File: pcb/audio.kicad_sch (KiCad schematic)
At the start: 30 parts, among them J4 AudioJack4, U4 ES7210, U5 ES8311, U6 IS31AP2005

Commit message: pcb: 473 cannot defeat me in any way that matters
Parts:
- J4: footprint Connector_Audio:Jack_3.5mm_PJ320D_Horizontal -> live-caption-badge:Jack_3.5mm_PJ320D_Horizontal
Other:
- title: (none) -> Live Caption Badge - Audio Subsystem
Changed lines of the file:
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@@
 	(generator_version "8.0")
 	(paper "A4")
+	(title_block
+		(title "Live Caption Badge - Audio Subsystem")
+		(date "2024-10-29")
+	)
 	(junction
 		(at 46.99 71.12)
@@
 			)
 		)
-		(property "Footprint" "Connector_Audio:Jack_3.5mm_PJ320D_Horizontal"
+		(property "Footprint" "live-caption-badge:Jack_3.5mm_PJ320D_Horizontal"
 			(at 158.75 129.54 0)
 			(effects

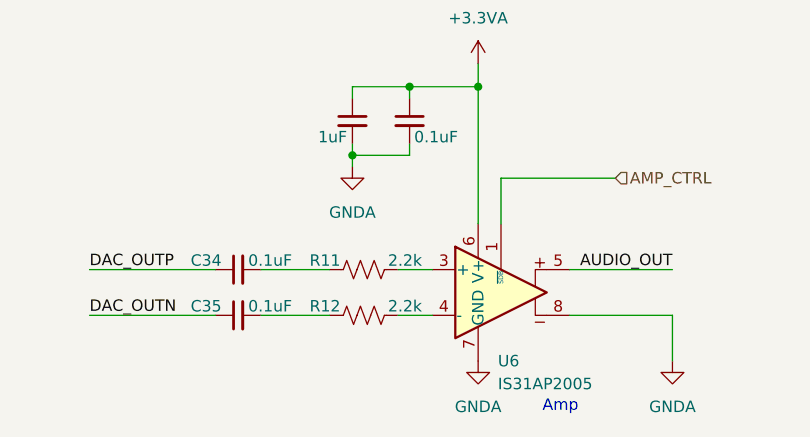
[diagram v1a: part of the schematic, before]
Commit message: pcb: Fix misc footprints, add silkprint
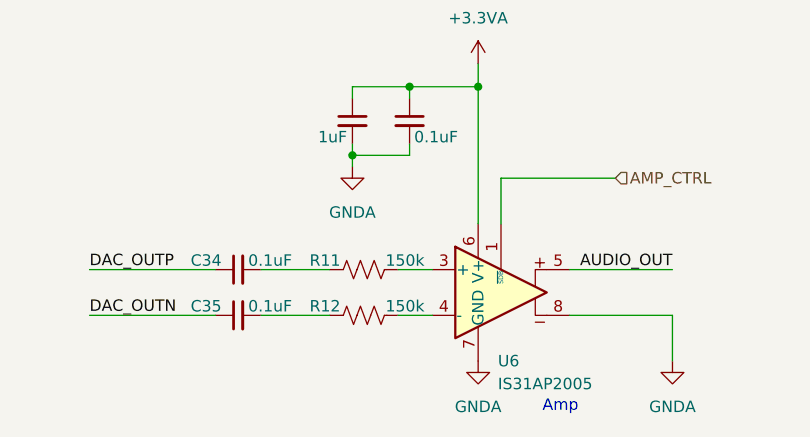
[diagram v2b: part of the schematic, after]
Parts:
- R11, R12: value 2.2k -> 150k
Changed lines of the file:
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@@
 			)
 		)
-		(property "Value" "2.2k"
+		(property "Value" "150k"
 			(at 78.232 141.224 90)
 			(effects
@@
 			)
 		)
-		(property "Value" "2.2k"
+		(property "Value" "150k"
 			(at 78.232 136.144 90)
 			(effects

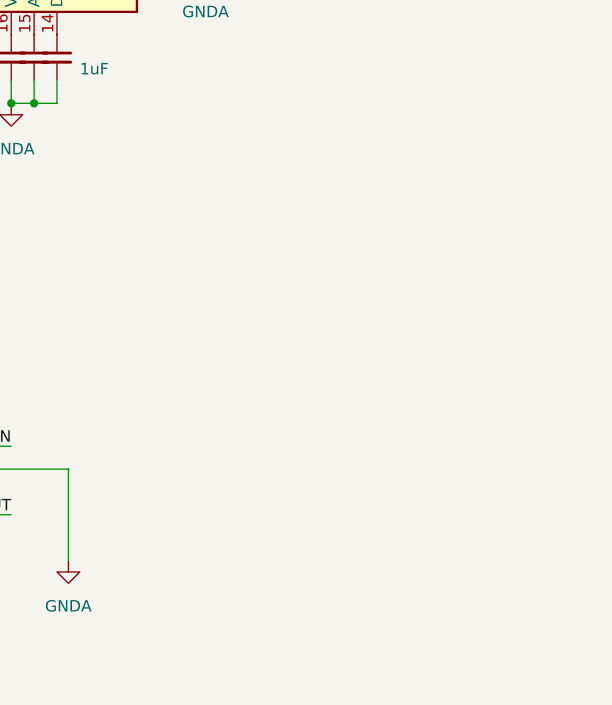
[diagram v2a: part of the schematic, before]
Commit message: pcb: Checkpoint before incorporating Mark and James' suggestions
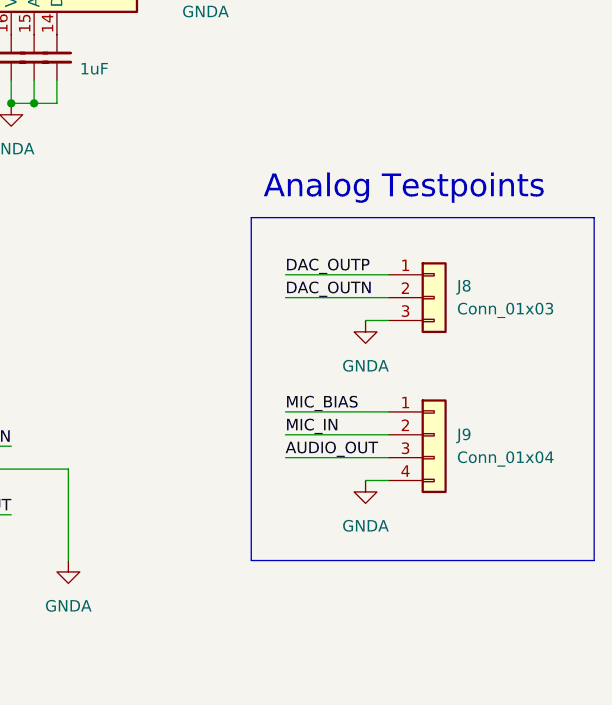
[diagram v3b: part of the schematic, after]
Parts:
- added J8: Conn_01x03, Connector_PinHeader_2.54mm:PinHeader_1x03_P2.54mm_Vertical, symbol Connector_Generic:Conn_01x03
- added J9: Conn_01x04, Connector_PinHeader_2.54mm:PinHeader_1x04_P2.54mm_Vertical, symbol Connector_Generic:Conn_01x04
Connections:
- net AUDIO_OUT: now also J9.3 (Pin_3)
- net DAC_OUTN: now also J8.2 (Pin_2)
- net DAC_OUTP: now also J8.1 (Pin_1)
- net GNDA: now also J8.3 (Pin_3), J9.4 (Pin_4)
- net MIC_BIAS: now also J9.1 (Pin_1)
- net MIC_IN: now also J9.2 (Pin_2)
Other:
- note added: "Analog Testpoints"

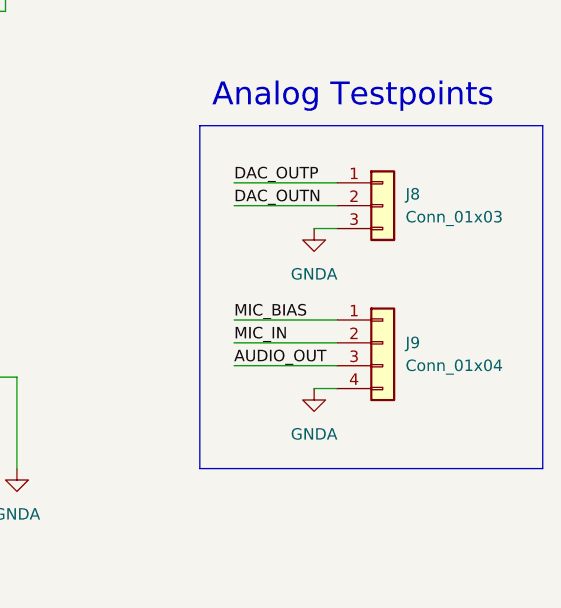
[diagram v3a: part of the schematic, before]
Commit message: pcb: Convert to 4-layer board
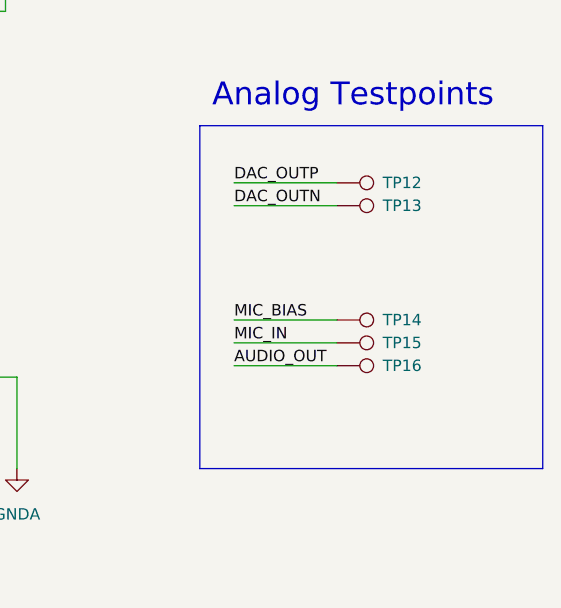
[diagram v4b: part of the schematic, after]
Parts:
- removed J8: Conn_01x03, Connector_PinHeader_2.54mm:PinHeader_1x03_P2.54mm_Vertical, symbol Connector_Generic:Conn_01x03
- removed J9: Conn_01x04, Connector_PinHeader_2.54mm:PinHeader_1x04_P2.54mm_Vertical, symbol Connector_Generic:Conn_01x04
- added TP12, TP13, TP14, TP15, TP16: TestPoint, Connector_PinHeader_2.54mm:PinHeader_1x01_P2.54mm_Vertical, symbol Connector:TestPoint
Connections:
- net AUDIO_OUT: now also TP16.1
- net DAC_OUTN: now also TP13.1
- net DAC_OUTP: now also TP12.1
- net MIC_BIAS: now also TP14.1
- net MIC_IN: now also TP15.1

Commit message: pcb: it may or may not work
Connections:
- net GNDA: now also U4.8 (GNDD)
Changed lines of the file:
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@@
 	)
 	(junction
-		(at 78.74 116.84)
+		(at 72.39 93.98)
 		(diameter 0)
 		(color 0 0 0 0)
 	)
 	(junction
-		(at 74.93 93.98)
+		(at 78.74 116.84)
 		(diameter 0)
 		(color 0 0 0 0)
@@
 		(color 0 0 0 0)
 	)
+	(junction
+		(at 74.93 93.98)
+		(diameter 0)
+		(color 0 0 0 0)
+	)
 	(no_connect
 		(at 60.96 58.42)
@@
 	(wire
 		(pts
+			(xy 72.39 91.44) (xy 72.39 93.98)
+		)
+		(stroke
+			(width 0)
+			(type default)
+		)
+	)
+	(wire
+		(pts
 			(xy 90.17 96.52) (xy 90.17 99.06)
 		)
@@
 	(wire
 		(pts
+			(xy 74.93 93.98) (xy 77.47 93.98)
+		)
+		(stroke
+			(width 0)
+			(type default)
+		)
+	)
+	(wire
+		(pts
 			(xy 176.53 88.9) (xy 176.53 86.36)
 		)
@@
 	(wire
 		(pts
-			(xy 74.93 93.98) (xy 74.93 99.06)
+			(xy 72.39 93.98) (xy 72.39 99.06)
 		)
 		(stroke
@@
 	(wire
 		(pts
-			(xy 77.47 93.98) (xy 74.93 93.98)
+			(xy 74.93 93.98) (xy 72.39 93.98)
 		)
 		(stroke
@@
 	(symbol
 		(lib_id "power:GNDA")
-		(at 74.93 99.06 0)
+		(at 72.39 99.06 0)
 		(unit 1)
 		(exclude_from_sim no)
@@
 		(fields_autoplaced yes)
 		(property "Reference" "#PWR042"
-			(at 74.93 105.41 0)
+			(at 72.39 105.41 0)
 			(effects
 				(font
@@
 		)
 		(property "Value" "GNDA"
-			(at 74.93 104.14 0)
+			(at 72.39 104.14 0)
 			(effects
 				(font
@@
 		)
 		(property "Footprint" ""
-			(at 74.93 99.06 0)
+			(at 72.39 99.06 0)
 			(effects
 				(font
@@
 		)
 		(property "Datasheet" ""
-			(at 74.93 99.06 0)
+			(at 72.39 99.06 0)
 			(effects
 				(font
@@
 		)
 		(property "Description" "Power symbol creates a global label with name \"GNDA\" , analog ground"
-			(at 74.93 99.06 0)
+			(at 72.39 99.06 0)
 			(effects
 				(font
@@
 		(pin "33"
 		)
+		(pin "8"
+		)
 		(instances

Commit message: pcb: Rev 2 schematic
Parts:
- added C6: 47uF, Capacitor_SMD:C_0603_1608Metric, symbol Device:C
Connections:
- net AUDIO_OUT: now also C6.2; no longer U6.5
- net GNDA: no longer U6.8
- new net: C6.1, U6.5
- no-connect marks 12 -> 13
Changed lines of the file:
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@@
 	)
 	(no_connect
+		(at 96.52 142.24)
+	)
+	(no_connect
 		(at 60.96 58.42)
 	)
@@
 	(wire
 		(pts
-			(xy 107.95 142.24) (xy 107.95 147.32)
-		)
-		(stroke
-			(width 0)
-			(type default)
-		)
-	)
-	(wire
-		(pts
 			(xy 82.55 99.06) (xy 85.09 99.06)
 		)
@@
 	(wire
 		(pts
-			(xy 96.52 142.24) (xy 107.95 142.24)
-		)
-		(stroke
-			(width 0)
-			(type default)
-		)
-	)
-	(wire
-		(pts
 			(xy 144.78 38.1) (xy 149.86 38.1)
 		)
@@
 	(wire
 		(pts
+			(xy 106.68 137.16) (xy 118.11 137.16)
+		)
+		(stroke
+			(width 0)
+			(type default)
+		)
+	)
+	(wire
+		(pts
 			(xy 139.7 71.12) (xy 149.86 71.12)
 		)
@@
 	(wire
 		(pts
-			(xy 96.52 137.16) (xy 107.95 137.16)
+			(xy 96.52 137.16) (xy 99.06 137.16)
 		)
 		(stroke
@@
 	)
 	(label "AUDIO_OUT"
-		(at 107.95 137.16 180)
+		(at 118.11 137.16 180)
 		(fields_autoplaced yes)
 		(effects
@@
 		(dnp no)
 		(property "Reference" "C16"
-			(at 152.4 34.2962 0)
+			(at 147.828 29.718 0)
 			(effects
 				(font
@@
 				)
 				(justify left)
-				(hide yes)
 			)
 		)
@@
 	)
 	(symbol
+		(lib_id "Device:C")
+		(at 102.87 137.16 90)
+		(unit 1)
+		(exclude_from_sim no)
+		(in_bom yes)
+		(on_board yes)
+		(dnp no)
+		(property "Reference" "C6"
+			(at 102.87 130.81 90)
+			(effects
+				(font
+					(size 1.27 1.27)
+				)
+			)
+		)
+		(property "Value" "47uF"
+			(at 102.87 133.35 90)
+			(effects
+				(font
+					(size 1.27 1.27)
+				)
+			)
+		)
+		(property "Footprint" "Capacitor_SMD:C_0603_1608Metric"
+			(at 106.68 136.1948 0)
+			(effects
+				(font
+					(size 1.27 1.27)
+				)
+				(hide yes)
+			)
+		)
+		(property "Datasheet" "~"
+			(at 102.87 137.16 0)
+			(effects
+				(font
+					(size 1.27 1.27)
+				)
+				(hide yes)
+			)
+		)
+		(property "Description" "Unpolarized capacitor"
+			(at 102.87 137.16 0)
+			(effects
+				(font
+					(size 1.27 1.27)
+				)
+				(hide yes)
+			)
+		)
+		(pin "1"
+		)
+		(pin "2"
+		)
+		(instances
+			(project ""
+				(path "/3b930924-1452-4d23-815e-09afbcdc5905/6626f702-51b6-4b1f-836e-d6234bc91af1"
+					(reference "C6")
+					(unit 1)
+				)
+			)
+		)
+	)
+	(symbol
 		(lib_id "power:GNDA")
 		(at 72.39 99.06 0)
@@
 		(dnp no)
 		(property "Reference" "C14"
-			(at 142.24 34.2962 0)
+			(at 137.668 29.718 0)
 			(effects
 				(font
@@
 				)
 				(justify left)
-				(hide yes)
 			)
 		)
@@
 	(symbol
 		(lib_id "power:GNDA")
-		(at 107.95 147.32 0)
-		(unit 1)
-		(exclude_from_sim no)
-		(in_bom yes)
-		(on_board yes)
-		(dnp no)
-		(fields_autoplaced yes)
-		(property "Reference" "#PWR048"
-			(at 107.95 153.67 0)
-			(effects
-				(font
-					(size 1.27 1.27)
-				)
-				(hide yes)
-			)
-		)
-		(property "Value" "GNDA"
-			(at 107.95 152.4 0)
-			(effects
-				(font
-					(size 1.27 1.27)
-				)
-			)
-		)
-		(property "Footprint" ""
-			(at 107.95 147.32 0)
-			(effects
-				(font
-					(size 1.27 1.27)
-				)
-				(hide yes)
-			)
-		)
-		(property "Datasheet" ""
-			(at 107.95 147.32 0)
-			(effects
-				(font
-					(size 1.27 1.27)
-				)
-				(hide yes)
-			)
-		)
-		(property "Description" "Power symbol creates a global label with name \"GNDA\" , analog ground"
-			(at 107.95 147.32 0)
-			(effects
-				(font
-					(size 1.27 1.27)
-				)
-				(hide yes)
-			)
-		)
-		(pin "1"
-		)
-		(instances
-			(project "live-caption-badge"
-				(path "/3b930924-1452-4d23-815e-09afbcdc5905/6626f702-51b6-4b1f-836e-d6234bc91af1"
-					(reference "#PWR048")
-					(unit 1)
-				)
-			)
-		)
-	)
-	(symbol
-		(lib_id "power:GNDA")
 		(at 86.36 147.32 0)
 		(unit 1)
@@
 		(dnp no)
 		(property "Reference" "C15"
-			(at 147.32 34.2962 0)
+			(at 142.748 29.718 0)
 			(effects
 				(font
@@
 				)
 				(justify left)
-				(hide yes)
 			)
 		)
@@
 		(dnp no)
 		(property "Reference" "C32"
-			(at 74.93 119.3862 0)
+			(at 68.326 118.872 0)
 			(effects
 				(font
@@
 				)
 				(justify left)
-				(hide yes)
 			)
 		)
@@
 		(dnp no)
 		(property "Reference" "C33"
-			(at 81.28 119.3862 0)
+			(at 78.994 118.872 0)
 			(effects
 				(font
@@
 				)
 				(justify left)
-				(hide yes)
 			)
 		)
@@
 		(on_board yes)
 		(dnp no)
-		(fields_autoplaced yes)
 		(property "Reference" "C24"
-			(at 179.07 82.5562 0)
+			(at 172.212 85.852 0)
 			(effects
 				(font
@@
 				)
 				(justify left)
-				(hide yes)
 			)
 		)

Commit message: pcb: rev 2?
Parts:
- added TP10, TP11, TP17, TP4, TP5, TP6, TP7, TP8, TP9: TestPoint, Connector_PinHeader_2.54mm:PinHeader_1x01_P2.54mm_Vertical, symbol Connector:TestPoint
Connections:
- net GNDA: now also TP11.1
- net I2C_SCL: now also TP10.1
- net I2C_SDA: now also TP9.1
- net I2S_LRCK: now also TP6.1
- net I2S_MCLK: now also TP4.1
- net I2S_SCLK: now also TP5.1
- net I2S_SDIN: now also TP8.1
- net I2S_SDOUT: now also TP7.1
- new net GND: TP17.1
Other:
- note added: "I2S & I2C Testpoints"
- moved on the sheet: TP12, TP13, TP14, TP15, TP16

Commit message: pcb: rev 2 ready?
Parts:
- added C48: 22pF, Capacitor_SMD:C_0603_1608Metric, symbol Device:C_Small
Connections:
- net GNDA: now also C48.2
- net MIC_IN: now also C48.1
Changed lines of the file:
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@@
 	(wire
 		(pts
+			(xy 185.42 135.89) (xy 185.42 139.7)
+		)
+		(stroke
+			(width 0)
+			(type default)
+		)
+	)
+	(wire
+		(pts
 			(xy 62.23 142.24) (xy 69.85 142.24)
 		)
@@
 	(wire
 		(pts
-			(xy 182.88 129.54) (xy 182.88 139.7)
+			(xy 179.07 129.54) (xy 179.07 139.7)
 		)
 		(stroke
@@
 	(wire
 		(pts
-			(xy 167.64 127) (xy 176.53 127)
+			(xy 167.64 127) (xy 185.42 127)
 		)
 		(stroke
@@
 	(wire
 		(pts
+			(xy 185.42 127) (xy 185.42 130.81)
+		)
+		(stroke
+			(width 0)
+			(type default)
+		)
+	)
+	(wire
+		(pts
 			(xy 194.31 71.12) (xy 198.12 71.12)
 		)
@@
 	(wire
 		(pts
-			(xy 163.83 129.54) (xy 182.88 129.54)
+			(xy 163.83 129.54) (xy 179.07 129.54)
 		)
 		(stroke
@@
 	)
 	(label "MIC_IN"
-		(at 176.53 127 180)
+		(at 185.42 127 180)
 		(fields_autoplaced yes)
 		(effects
@@
 	(symbol
 		(lib_id "power:GNDA")
-		(at 182.88 139.7 0)
+		(at 179.07 139.7 0)
 		(unit 1)
 		(exclude_from_sim no)
@@
 		(fields_autoplaced yes)
 		(property "Reference" "#PWR046"
-			(at 182.88 146.05 0)
+			(at 179.07 146.05 0)
 			(effects
 				(font
@@
 		)
 		(property "Value" "GNDA"
-			(at 182.88 144.78 0)
+			(at 179.07 144.78 0)
 			(effects
 				(font
@@
 		)
 		(property "Footprint" ""
-			(at 182.88 139.7 0)
+			(at 179.07 139.7 0)
 			(effects
 				(font
@@
 		)
 		(property "Datasheet" ""
-			(at 182.88 139.7 0)
+			(at 179.07 139.7 0)
 			(effects
 				(font
@@
 		)
 		(property "Description" "Power symbol creates a global label with name \"GNDA\" , analog ground"
-			(at 182.88 139.7 0)
+			(at 179.07 139.7 0)
 			(effects
 				(font
@@
 	)
 	(symbol
+		(lib_id "power:GNDA")
+		(at 185.42 139.7 0)
+		(unit 1)
+		(exclude_from_sim no)
+		(in_bom yes)
+		(on_board yes)
+		(dnp no)
+		(fields_autoplaced yes)
+		(property "Reference" "#PWR049"
+			(at 185.42 146.05 0)
+			(effects
+				(font
+					(size 1.27 1.27)
+				)
+				(hide yes)
+			)
+		)
+		(property "Value" "GNDA"
+			(at 185.42 144.78 0)
+			(effects
+				(font
+					(size 1.27 1.27)
+				)
+			)
+		)
+		(property "Footprint" ""
+			(at 185.42 139.7 0)
+			(effects
+				(font
+					(size 1.27 1.27)
+				)
+				(hide yes)
+			)
+		)
+		(property "Datasheet" ""
+			(at 185.42 139.7 0)
+			(effects
+				(font
+					(size 1.27 1.27)
+				)
+				(hide yes)
+			)
+		)
+		(property "Description" "Power symbol creates a global label with name \"GNDA\" , analog ground"
+			(at 185.42 139.7 0)
+			(effects
+				(font
+					(size 1.27 1.27)
+				)
+				(hide yes)
+			)
+		)
+		(pin "1"
+		)
+		(instances
+			(project "live-caption-badge"
+				(path "/3b930924-1452-4d23-815e-09afbcdc5905/6626f702-51b6-4b1f-836e-d6234bc91af1"
+					(reference "#PWR049")
+					(unit 1)
+				)
+			)
+		)
+	)
+	(symbol
 		(lib_id "Device:C_Small")
 		(at 198.12 67.31 0)
@@
 					(unit 1)
 				)
+			)
+		)
+	)
+	(symbol
+		(lib_id "Device:C_Small")
+		(at 185.42 133.35 0)
+		(unit 1)
+		(exclude_from_sim no)
+		(in_bom yes)
+		(on_board yes)
+		(dnp no)
+		(fields_autoplaced yes)
+		(property "Reference" "C48"
+			(at 187.96 132.0862 0)
+			(effects
+				(font
+					(size 1.27 1.27)
+				)
+				(justify left)
+			)
+		)
+		(property "Value" "22pF"
+			(at 187.96 134.6262 0)
+			(effects
+				(font
+					(size 1.27 1.27)
+				)
+				(justify left)
+			)
+		)
+		(property "Footprint" "Capacitor_SMD:C_0603_1608Metric"
+			(at 185.42 133.35 0)
+			(effects
+				(font
+					(size 1.27 1.27)
+				)
+				(hide yes)
+			)
+		)
+		(property "Datasheet" "~"
+			(at 185.42 133.35 0)
+			(effects
+				(font
+					(size 1.27 1.27)
+				)
+				(hide yes)
+			)
+		)
+		(property "Description" "Unpolarized capacitor, small symbol"
+			(at 185.42 133.35 0)
+			(effects
+				(font
+					(size 1.27 1.27)
+				)
+				(hide yes)
+			)
+		)
+		(pin "1"
+		)
+		(pin "2"
+		)
+		(instances
+			(project "live-caption-badge"
+				(path "/3b930924-1452-4d23-815e-09afbcdc5905/6626f702-51b6-4b1f-836e-d6234bc91af1"
+					(reference "C48")
+					(unit 1)
+				)
